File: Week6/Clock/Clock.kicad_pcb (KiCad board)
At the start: 2 copper layers, 140 x 90 mm, 50 parts, among them J1 Power_inlet_vertical, J2 Conn_01x06, SW1 RotaryEncoder_Switch, SW2 Omron_B3F_SPST, U2 ATmega328-PU, U3 L7805_TO92, U4 DS1307_DIP-8, U5 MAX7219, U6 MAX7219, Y1 Crystal 16MHZ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

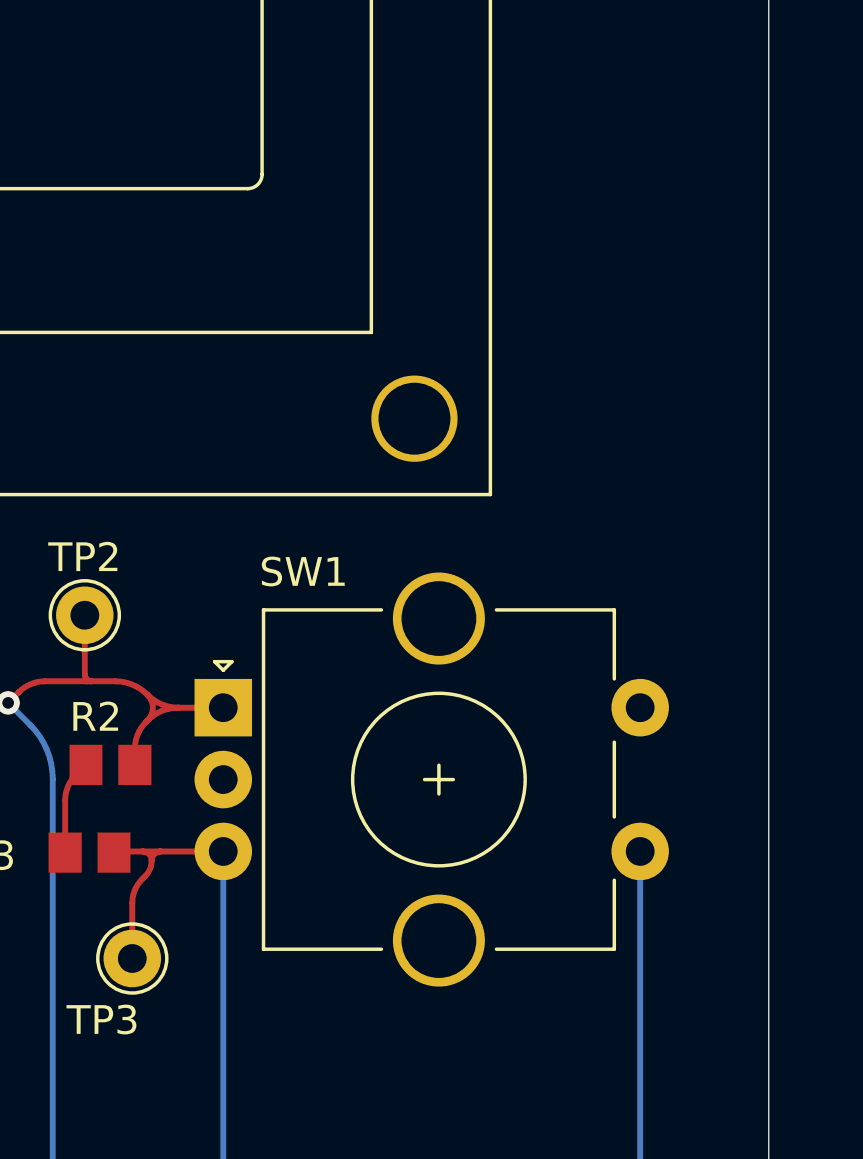
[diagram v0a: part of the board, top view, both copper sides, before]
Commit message: Rot Encoder Update
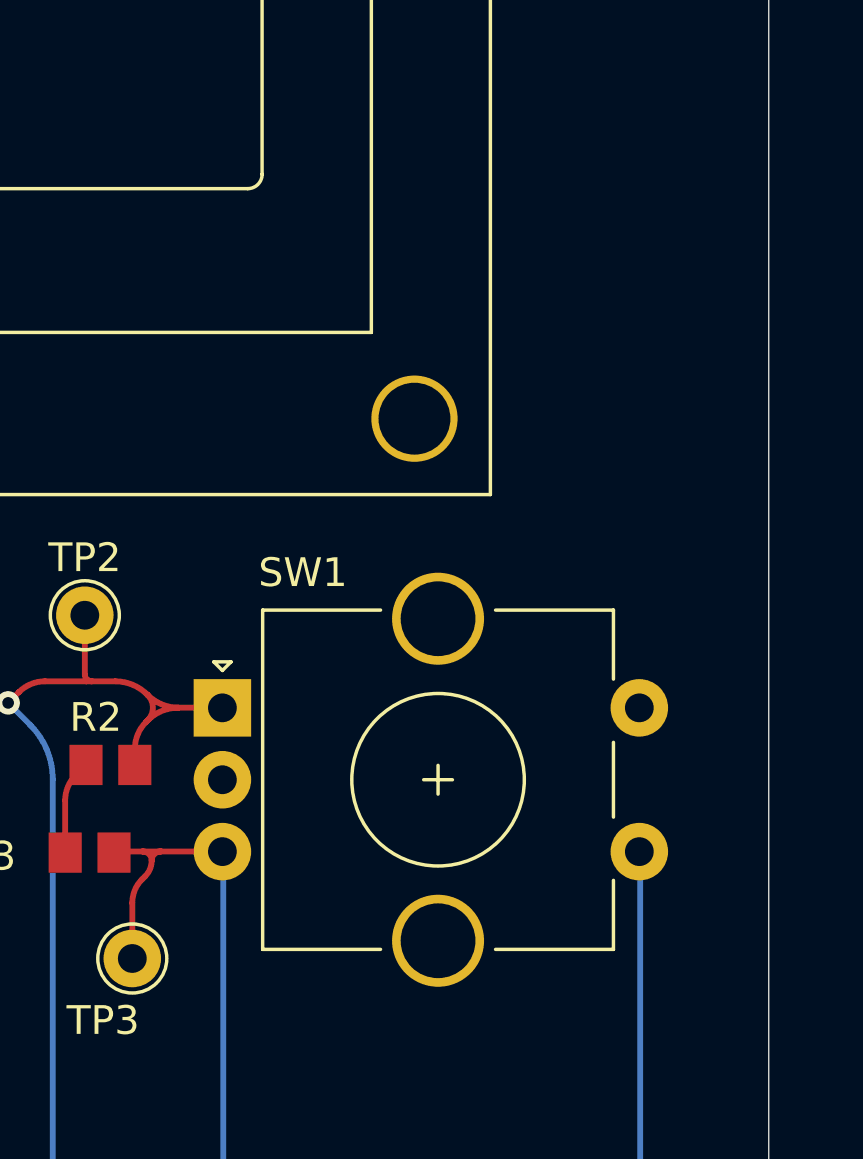
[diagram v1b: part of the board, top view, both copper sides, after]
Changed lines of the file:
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@@
       (viasonmask false)
       (mode 1)
-      (useauxorigin false)
+      (useauxorigin true)
       (hpglpennumber 1)
       (hpglpenspeed 20)
@@
       (psa4output false)
       (plotreference true)
-      (plotvalue true)
+      (plotvalue false)
       (plotinvisibletext false)
       (sketchpadsonfab false)
-      (subtractmaskfromsilk false)
+      (subtractmaskfromsilk true)
       (outputformat 1)
       (mirror false)
-      (drillshape 1)
+      (drillshape 0)
       (scaleselection 1)
-      (outputdirectory "")
+      (outputdirectory "gerbers/")
     )
   )
@@
     )
   )
+  (footprint "footprints:RotaryEncoder_TT_EN11-Switch_Vertical_H20mm_CircularMountingHoles" (layer "F.Cu")
+    (at 201 101.9)
+    (descr "Alps rotary encoder, EC12E... with switch, vertical shaft, mounting holes with circular drills, http://www.alps.com/prod/info/E/HTML/Encoder/Incremental/EC11/EC11E15204A3.html")
+    (tags "rotary encoder")
+    (property "Digikey PN" "987-1188-ND")
+    (property "Sheetfile" "Clock.kicad_sch")
+    (property "Sheetname" "")
+    (attr through_hole)
+    (fp_text reference "SW1" (at 2.8 -4.7) (layer "F.SilkS")
+      (effects (font (size 1 1) (thickness 0.15)))
+    )
+    (fp_text value "RotaryEncoder_Switch" (at 7.5 10.4) (layer "F.Fab")
+      (effects (font (size 1 1) (thickness 0.15)))
+    )
+    (fp_text user "${REFERENCE}" (at 11.1 6.3) (layer "F.Fab")
+      (effects (font (size 1 1) (thickness 0.15)))
+    )
+    (fp_line (start 0.3 -1.6) (end 0 -1.3) (layer "F.SilkS") (width 0.12))
+    (fp_line (start 5.5 -3.4) (end 1.4 -3.4) (layer "F.SilkS") (width 0.12))
+    (fp_line (start 1.4 -3.4) (end 1.4 8.4) (layer "F.SilkS") (width 0.12))
+    (fp_line (start 13.6 -3.4) (end 13.6 -1) (layer "F.SilkS") (width 0.12))
+    (fp_line (start -0.3 -1.6) (end 0.3 -1.6) (layer "F.SilkS") (width 0.12))
+    (fp_line (start 7 2.5) (end 8 2.5) (layer "F.SilkS") (width 0.12))
+    (fp_line (start 13.6 6) (end 13.6 8.4) (layer "F.SilkS") (width 0.12))
+    (fp_line (start 13.6 8.4) (end 9.5 8.4) (layer "F.SilkS") (width 0.12))
+    (fp_line (start 0 -1.3) (end -0.3 -1.6) (layer "F.SilkS") (width 0.12))
+    (fp_line (start 9.5 -3.4) (end 13.6 -3.4) (layer "F.SilkS") (width 0.12))
+    (fp_line (start 5.5 8.4) (end 1.4 8.4) (layer "F.SilkS") (width 0.12))
+    (fp_line (start 13.6 1.2) (end 13.6 3.8) (layer "F.SilkS") (width 0.12))
+    (fp_line (start 7.5 2) (end 7.5 3) (layer "F.SilkS") (width 0.12))
+    (fp_circle (center 7.5 2.5) (end 10.5 2.5) (layer "F.SilkS") (width 0.12) (fill none))
+    (fp_line (start -1.5 -5.2) (end 16 -5.2) (layer "F.CrtYd") (width 0.05))
+    (fp_line (start -1.5 -5.2) (end -1.5 10.2) (layer "F.CrtYd") (width 0.05))
+    (fp_line (start 16 10.2) (end 16 -5.2) (layer "F.CrtYd") (width 0.05))
+    (fp_line (start 16 10.2) (end -1.5 10.2) (layer "F.CrtYd") (width 0.05))
+    (fp_line (start 4.5 2.5) (end 10.5 2.5) (layer "F.Fab") (width 0.12))
+    (fp_line (start 7.5 -0.5) (end 7.5 5.5) (layer "F.Fab") (width 0.12))
+    (fp_line (start 13.5 -3.3) (end 13.5 8.3) (layer "F.Fab") (width 0.12))
+    (fp_line (start 13.5 8.3) (end 1.5 8.3) (layer "F.Fab") (width 0.12))
+    (fp_line (start 1.5 -2.2) (end 2.5 -3.3) (layer "F.Fab") (width 0.12))
+    (fp_line (start 2.5 -3.3) (end 13.5 -3.3) (layer "F.Fab") (width 0.12))
+    (fp_line (start 1.5 8.3) (end 1.5 -2.2) (layer "F.Fab") (width 0.12))
+    (fp_circle (center 7.5 2.5) (end 10.5 2.5) (layer "F.Fab") (width 0.12) (fill none))
+    (pad "" thru_hole circle (at 7.5 -3.1) (size 3.2 3.2) (drill 2.6) (layers *.Cu *.Mask))
+    (pad "" thru_hole circle (at 7.5 8.1) (size 3.2 3.2) (drill 2.6) (layers *.Cu *.Mask))
+    (pad "A" thru_hole rect (at 0 0) (size 2 2) (drill 1) (layers *.Cu *.Mask)
+      (net 42 "ROT ENC A OUT") (pinfunction "A") (pintype "passive"))
+    (pad "B" thru_hole circle (at 0 5) (size 2 2) (drill 1) (layers *.Cu *.Mask)
+      (net 43 "ROT ENC B OUT") (pinfunction "B") (pintype "passive"))
+    (pad "C" thru_hole circle (at 0 2.5) (size 2 2) (drill 1) (layers *.Cu *.Mask)
+      (net 6 "GND") (pinfunction "C") (pintype "passive"))
+    (pad "S1" thru_hole circle (at 14.5 5) (size 2 2) (drill 1) (layers *.Cu *.Mask)
+      (net 11 "ROT ENC SWITCH") (pinfunction "S1") (pintype "passive"))
+    (pad "S2" thru_hole circle (at 14.5 0) (size 2 2) (drill 1) (layers *.Cu *.Mask)
+      (net 6 "GND") (pinfunction "S2") (pintype "passive"))
+    (model "${HPS3DMOD}/EN11-HSM1AF15--.STEP"
+      (offset (xyz 7.5 -2.5 0.5))
+      (scale (xyz 1 1 1))
+      (rotate (xyz -90 0 90))
+    )
+  )
   (footprint "footprints:KWM-30881CVB" (layer "F.Cu")
     (at 106.618 124.714)
@@
     (fp_arc (start 63.7 8) (mid 64.053553 8.146447) (end 64.2 8.5) (layer "F.SilkS") (width 0.12))
     (fp_arc (start 0.20066 22.9997) (mid -0.153162 22.853142) (end -0.29972 22.49932) (layer "F.SilkS") (width 0.12))
-    (fp_arc (start 64.20104 22.49932) (mid 64.054473 22.853115) (end 63.70066 22.9997) (layer "F.SilkS") (width 0.12))
+    (fp_arc (start 64.20104 22.49932) (mid 64.054479 22.85315) (end 63.70066 22.9997) (layer "F.SilkS") (width 0.12))
     (fp_line (start -8.25 -2.75) (end 72.25 -2.75) (layer "F.CrtYd") (width 0.05))
     (fp_line (start -8.25 33.75) (end 72.25 33.75) (layer "F.CrtYd") (width 0.05))
@@
     )
   )
-  (footprint "footprints:RotaryEncoder_TT_EN11-Switch_Vertical_H20mm_CircularMountingHoles" (layer "F.Cu")
-    (at 201.03 101.894)
-    (descr "Alps rotary encoder, EC12E... with switch, vertical shaft, mounting holes with circular drills, http://www.alps.com/prod/info/E/HTML/Encoder/Incremental/EC11/EC11E15204A3.html")
-    (tags "rotary encoder")
-    (property "Digikey PN" "987-1398-ND ")
-    (property "Sheetfile" "Clock.kicad_sch")
-    (property "Sheetname" "")
-    (attr through_hole)
-    (fp_text reference "SW1" (at 2.8 -4.7) (layer "F.SilkS")
-      (effects (font (size 1 1) (thickness 0.15)))
-    )
-    (fp_text value "RotaryEncoder_Switch" (at 7.5 10.4) (layer "F.Fab")
-      (effects (font (size 1 1) (thickness 0.15)))
-    )
-    (fp_text user "${REFERENCE}" (at 11.1 6.3) (layer "F.Fab")
-      (effects (font (size 1 1) (thickness 0.15)))
-    )
-    (fp_line (start 13.6 1.2) (end 13.6 3.8) (layer "F.SilkS") (width 0.12))
-    (fp_line (start 9.5 -3.4) (end 13.6 -3.4) (layer "F.SilkS") (width 0.12))
-    (fp_line (start 0.3 -1.6) (end 0 -1.3) (layer "F.SilkS") (width 0.12))
-    (fp_line (start 0 -1.3) (end -0.3 -1.6) (layer "F.SilkS") (width 0.12))
-    (fp_line (start 13.6 6) (end 13.6 8.4) (layer "F.SilkS") (width 0.12))
-    (fp_line (start 13.6 -3.4) (end 13.6 -1) (layer "F.SilkS") (width 0.12))
-    (fp_line (start 5.5 8.4) (end 1.4 8.4) (layer "F.SilkS") (width 0.12))
-    (fp_line (start -0.3 -1.6) (end 0.3 -1.6) (layer "F.SilkS") (width 0.12))
-    (fp_line (start 1.4 -3.4) (end 1.4 8.4) (layer "F.SilkS") (width 0.12))
-    (fp_line (start 7.5 2) (end 7.5 3) (layer "F.SilkS") (width 0.12))
-    (fp_line (start 5.5 -3.4) (end 1.4 -3.4) (layer "F.SilkS") (width 0.12))
-    (fp_line (start 13.6 8.4) (end 9.5 8.4) (layer "F.SilkS") (width 0.12))
-    (fp_line (start 7 2.5) (end 8 2.5) (layer "F.SilkS") (width 0.12))
-    (fp_circle (center 7.5 2.5) (end 10.5 2.5) (layer "F.SilkS") (width 0.12) (fill none))
-    (fp_line (start 16 10.2) (end -1.5 10.2) (layer "F.CrtYd") (width 0.05))
-    (fp_line (start -1.5 -5.2) (end 16 -5.2) (layer "F.CrtYd") (width 0.05))
-    (fp_line (start 16 10.2) (end 16 -5.2) (layer "F.CrtYd") (width 0.05))
-    (fp_line (start -1.5 -5.2) (end -1.5 10.2) (layer "F.CrtYd") (width 0.05))
-    (fp_line (start 4.5 2.5) (end 10.5 2.5) (layer "F.Fab") (width 0.12))
-    (fp_line (start 7.5 -0.5) (end 7.5 5.5) (layer "F.Fab") (width 0.12))
-    (fp_line (start 13.5 -3.3) (end 13.5 8.3) (layer "F.Fab") (width 0.12))
-    (fp_line (start 13.5 8.3) (end 1.5 8.3) (layer "F.Fab") (width 0.12))
-    (fp_line (start 2.5 -3.3) (end 13.5 -3.3) (layer "F.Fab") (width 0.12))
-    (fp_line (start 1.5 -2.2) (end 2.5 -3.3) (layer "F.Fab") (width 0.12))
-    (fp_line (start 1.5 8.3) (end 1.5 -2.2) (layer "F.Fab") (width 0.12))
-    (fp_circle (center 7.5 2.5) (end 10.5 2.5) (layer "F.Fab") (width 0.12) (fill none))
-    (pad "A" thru_hole rect (at 0 0) (size 2 2) (drill 1) (layers *.Cu *.Mask)
-      (net 42 "ROT ENC A OUT") (pinfunction "A") (pintype "passive"))
-    (pad "B" thru_hole circle (at 0 5) (size 2 2) (drill 1) (layers *.Cu *.Mask)
-      (net 43 "ROT ENC B OUT") (pinfunction "B") (pintype "passive"))
-    (pad "C" thru_hole circle (at 0 2.5) (size 2 2) (drill 1) (layers *.Cu *.Mask)
-      (net 6 "GND") (pinfunction "C") (pintype "passive"))
-    (pad "MP" thru_hole circle (at 7.5 -3.1) (size 3.2 3.2) (drill 2.6) (layers *.Cu *.Mask))
-    (pad "MP" thru_hole circle (at 7.5 8.1) (size 3.2 3.2) (drill 2.6) (layers *.Cu *.Mask))
-    (pad "S1" thru_hole circle (at 14.5 5) (size 2 2) (drill 1) (layers *.Cu *.Mask)
-      (net 11 "ROT ENC SWITCH") (pinfunction "S1") (pintype "passive"))
-    (pad "S2" thru_hole circle (at 14.5 0) (size 2 2) (drill 1) (layers *.Cu *.Mask)
-      (net 6 "GND") (pinfunction "S2") (pintype "passive"))
-    (model "${HPS3DMOD}/EN11-HSM1BF20--.STEP"
-      (offset (xyz 7.5 -2.5 6.2))
-      (scale (xyz 1 1 1))
-      (rotate (xyz -90 0 90))
-    )
-  )
